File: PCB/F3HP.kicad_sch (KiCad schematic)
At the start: 103 parts, among them J1 L_In, J2 R_In, J3 HPOut, J4 AC_In, J5 Switch, K1 C93402, Q1 BC850C, Q2 BC860C, Q3 BCP56TA, Q4 BC850C, Q5 BC860C, Q6 BCP56TA, Q7 BC850C, Q8 AO3400A, Q9 BC860C, U1 TPS7A4701

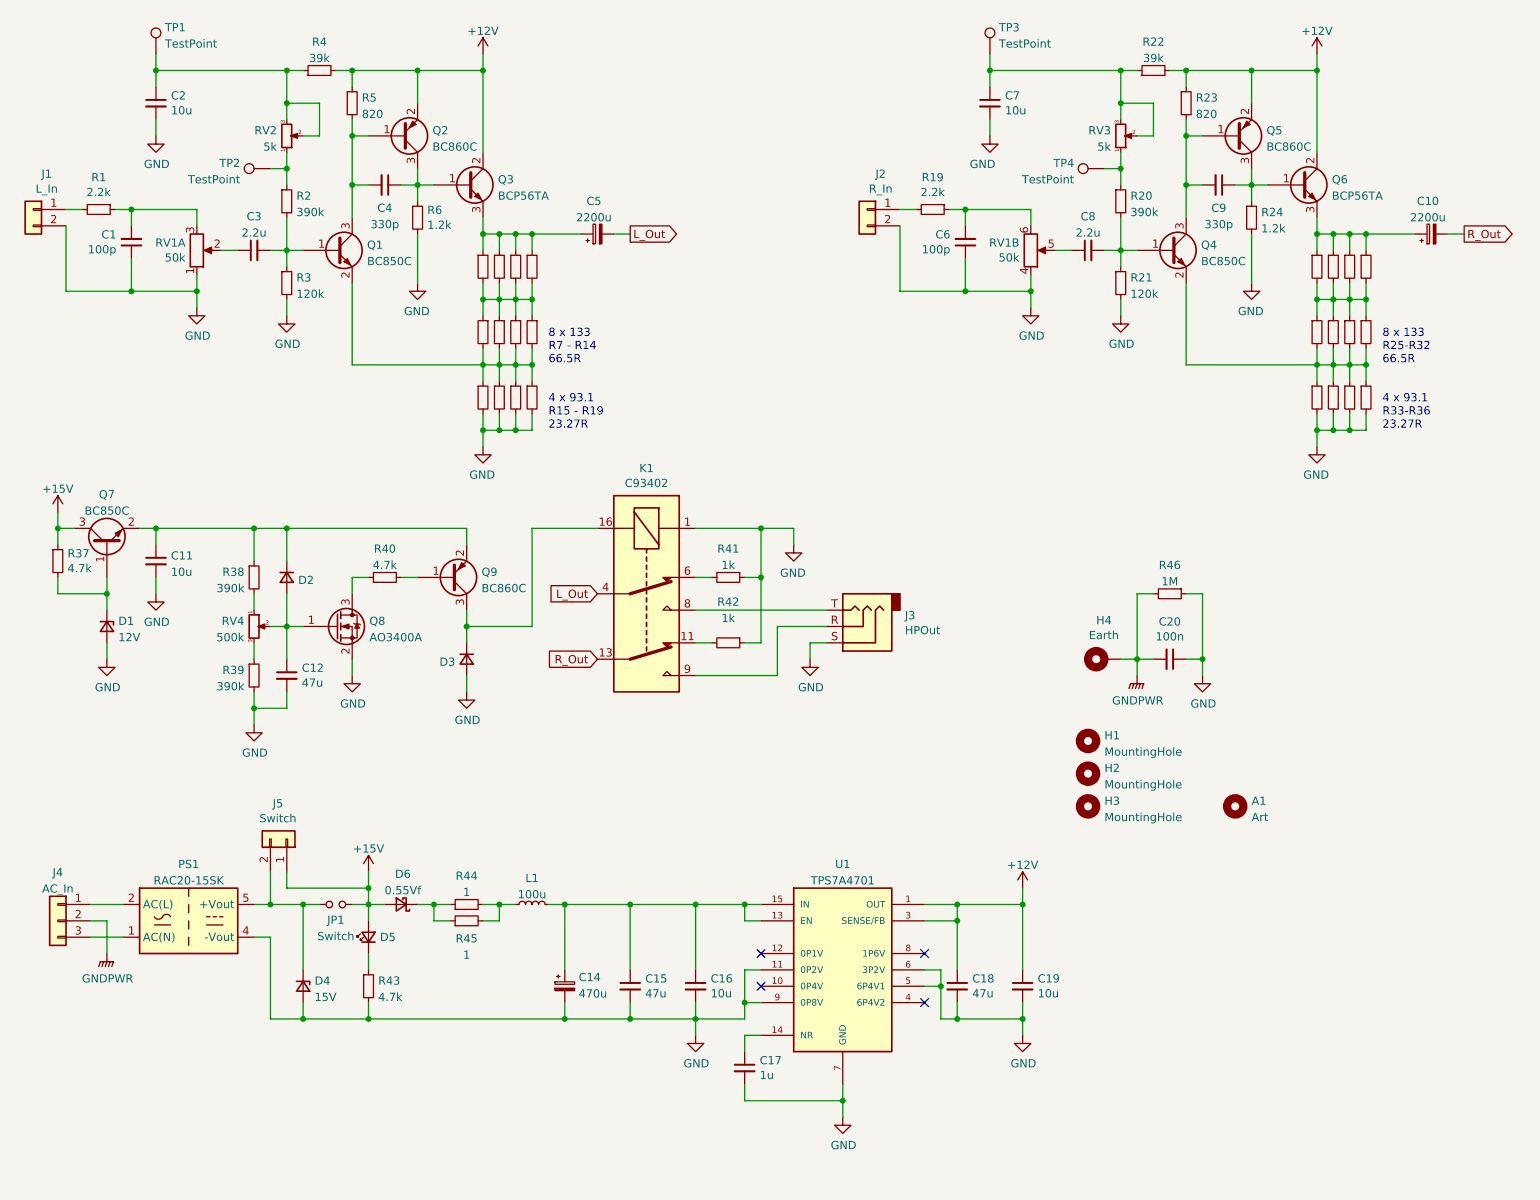
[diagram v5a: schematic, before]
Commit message: Changed resistors to 1206 to lower distortion
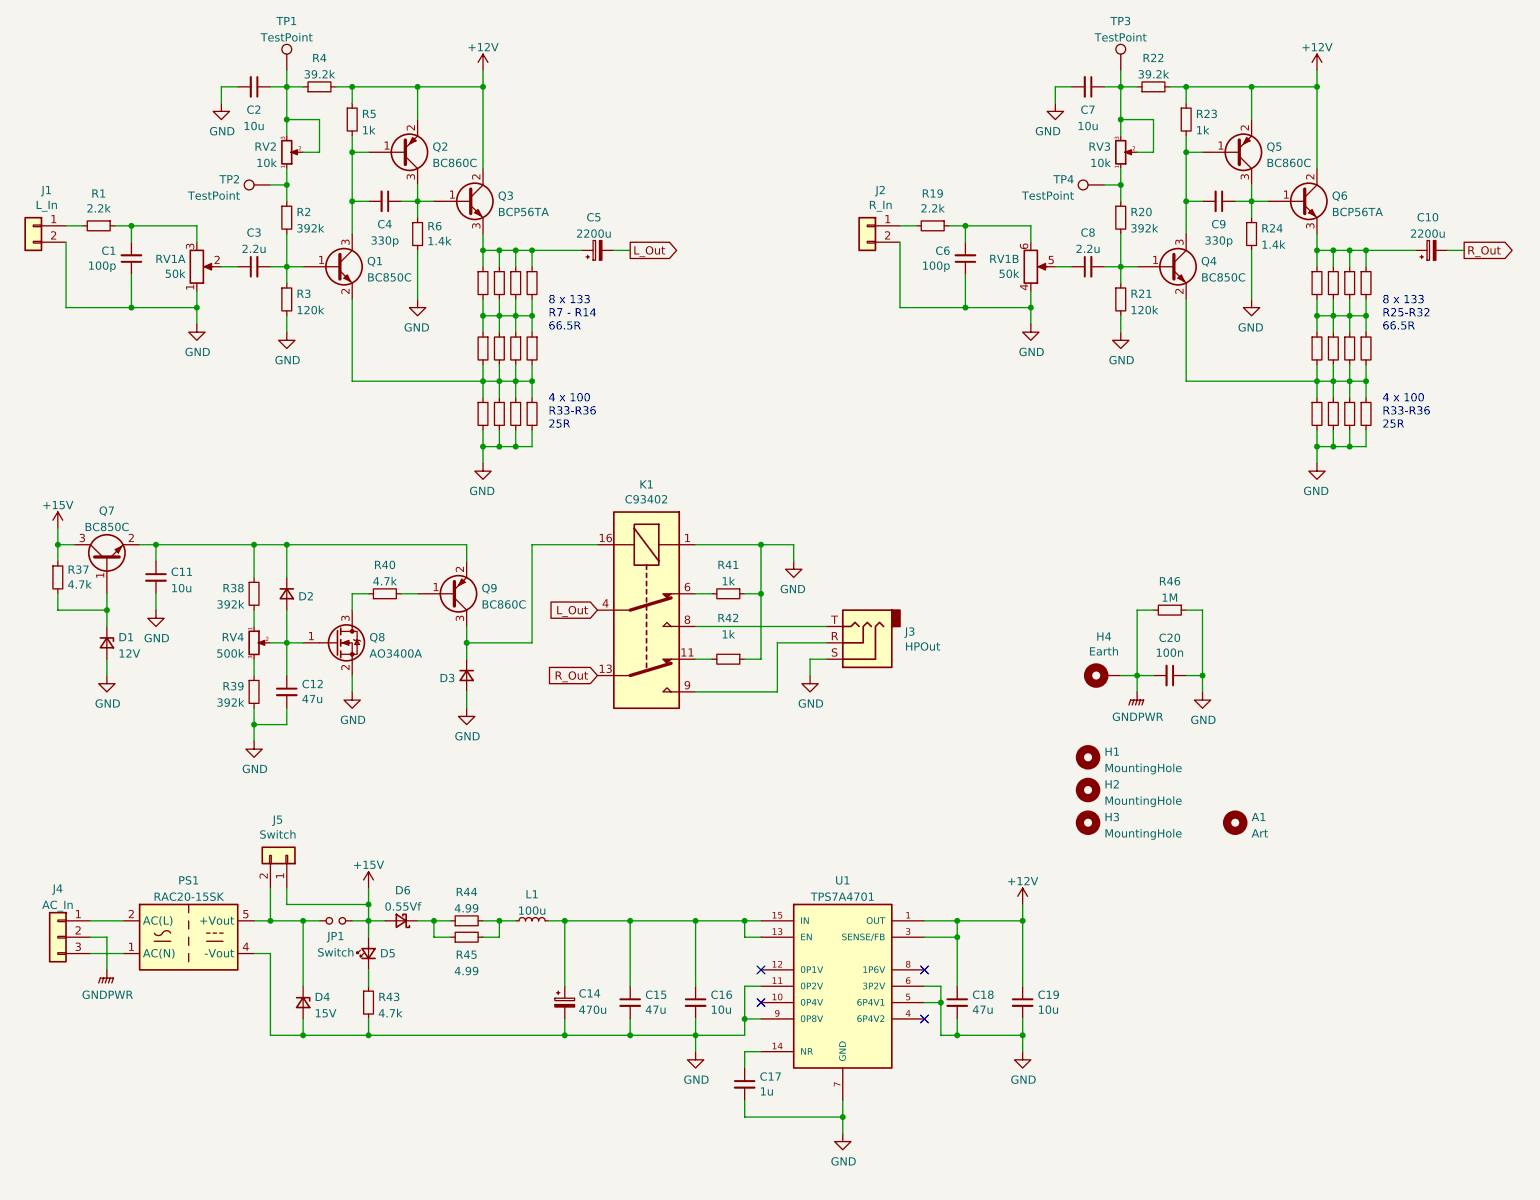
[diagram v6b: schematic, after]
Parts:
- C14: LCSC part number (none) -> C193277; Part number (none) -> EEEFT1E471GP
- R1, R19: footprint Resistor_SMD:R_0603_1608Metric -> Resistor_SMD:R_1206_3216Metric; LCSC part number C706068 -> (none); Part number RT0603DRE072K2L -> RT1206FRE072K2L
- R10, R11, R12, R13, R14, R25, R26, R27, R28, R29, R30, R31, R32, R7, R8, R9: LCSC part number C872564 -> (none)
- R15, R16, R17, R18, R33, R34, R35, R36: value 93.1 -> 100; LCSC part number C706437 -> (none); Part number RT1206FRE0793R1L -> RT1206DRD07100RL
- R2, R20, R38, R39: value 390k -> 392k; footprint Resistor_SMD:R_0603_1608Metric -> Resistor_SMD:R_1206_3216Metric; LCSC part number C862701 -> (none); Part number RT0603DRD07390KL -> RT1206BRD07392KL
- R21, R3: footprint Resistor_SMD:R_0603_1608Metric -> Resistor_SMD:R_1206_3216Metric; LCSC part number C706020 -> C136888; Part number RT0603DRE07120KL -> RT1206BRD07120KL
- R22, R4: value 39k -> 39.2k; footprint Resistor_SMD:R_0603_1608Metric -> Resistor_SMD:R_1206_3216Metric; LCSC part number C705983 -> (none); Part number RT0603DRD0739RL -> RT1206DRD0739K2L
- R23, R5: value 820 -> 1k; footprint Resistor_SMD:R_0603_1608Metric -> Resistor_SMD:R_1206_3216Metric; LCSC part number C723589 -> C706405; Part number RT0603DRD07820RL -> RT1206BRD071KL
- R24, R6: value 1.2k -> 1.4k; footprint Resistor_SMD:R_0603_1608Metric -> Resistor_SMD:R_1206_3216Metric; LCSC part number C723656 -> C870504; Part number RT0603DRD071K2L -> RT1206BRD071K4L
- R37, R40, R43: footprint Resistor_SMD:R_0603_1608Metric -> Resistor_SMD:R_1206_3216Metric; LCSC part number C513565 -> C706416; Part number RT0603BRD074K7L -> RT1206BRD074K64L
- R41, R42: footprint Resistor_SMD:R_0603_1608Metric -> Resistor_SMD:R_1206_3216Metric; LCSC part number C706049 -> C706405; Part number RT0603DRE071KL -> RT1206BRD071KL
- R44, R45: value 1 -> 4.99; LCSC part number C728690 -> C326584; Part number RT1206FRE071RL -> RT1206BRD074R99L
- R46: footprint Resistor_SMD:R_0603_1608Metric -> Resistor_SMD:R_1206_3216Metric; LCSC part number C862961 -> C375528; Part number RT0603DRE071ML -> RT1206FRE071ML
- RV2, RV3: value 5k -> 10k; LCSC part number C780226 -> C780232; Part number 3266W-1-503LF -> 3266W-1-104LF
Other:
- note added: "4 x 100 R33-R36 25R"
- note removed: "4 x 93.1 R15 - R19 23.27R"
- note removed: "4 x 93.1 R33-R36 23.27R"
- moved on the sheet: A1, C1, C10, C11, C12, C14, C15, C16, C17, C18, C19, C2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
